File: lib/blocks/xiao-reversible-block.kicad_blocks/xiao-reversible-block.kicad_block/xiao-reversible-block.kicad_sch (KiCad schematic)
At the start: 34 parts, among them J1 Conn_01x02, U1 XIAO-nRF52840-DIP

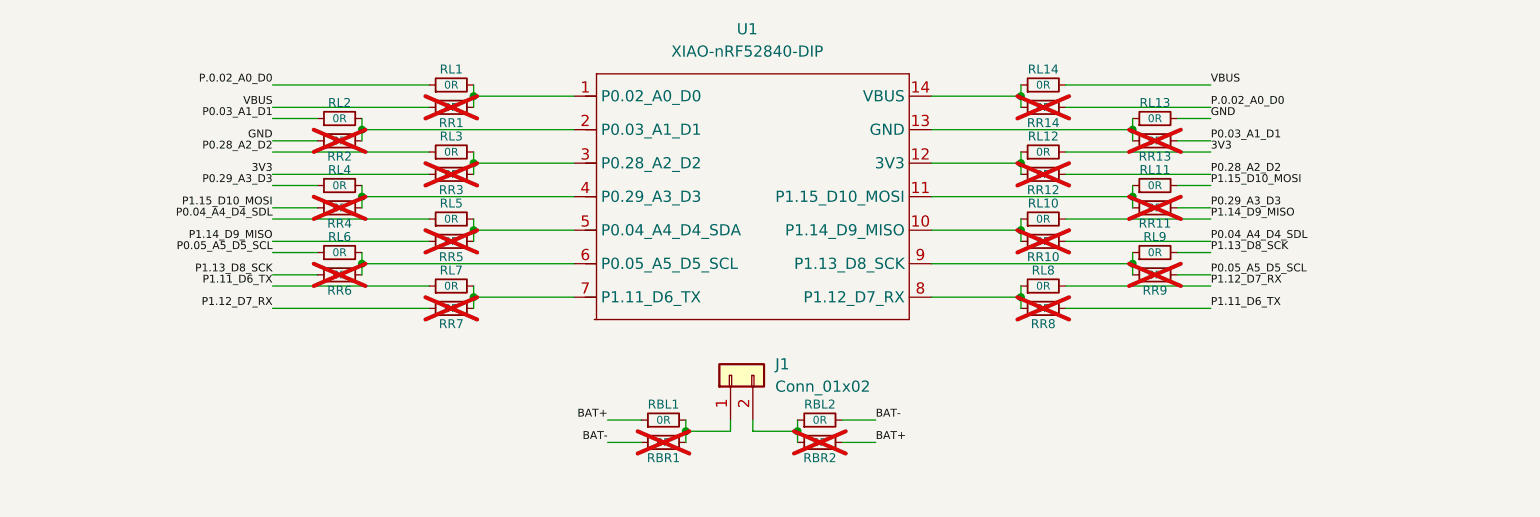
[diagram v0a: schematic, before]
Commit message: fix: fix bugs and improve
- typo: SDL -> SDA
- replaced GND net by actual ground symbol
- fixed power flags for ERC
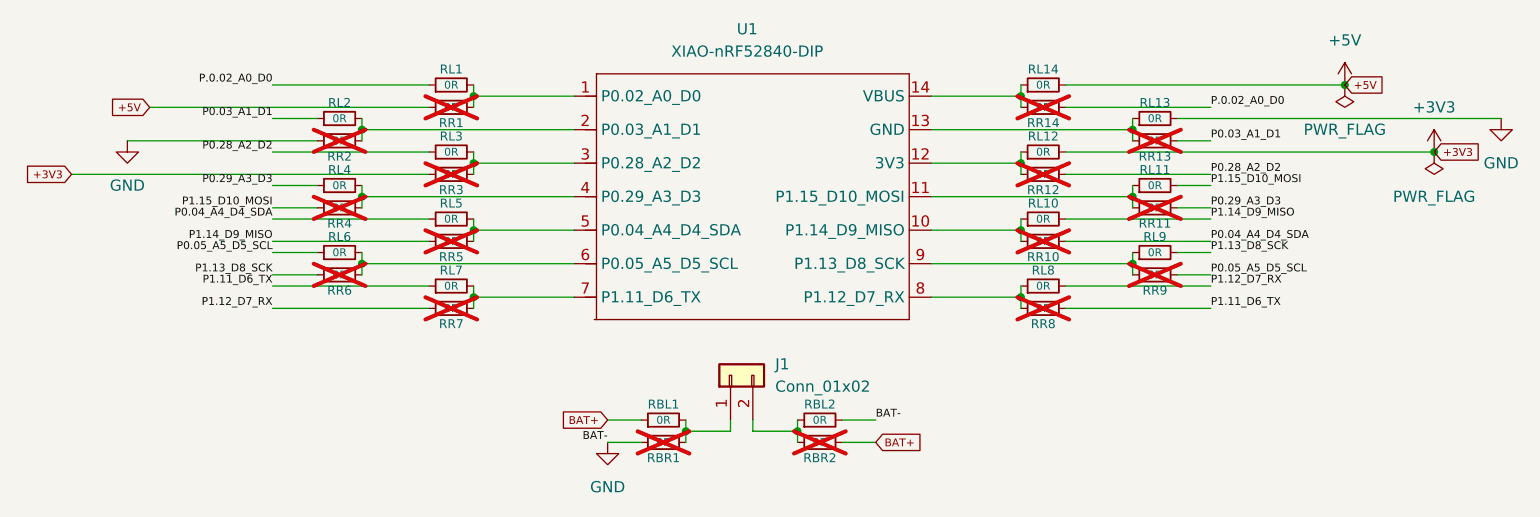
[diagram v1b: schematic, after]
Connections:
- net BAT- is gone; now on net GND: RBL2.2, RBR1.2
- net 3V3 renamed +3V3
- net P0.04_A4_D4_SDL renamed P0.04_A4_D4_SDA
- net VBUS renamed +5V
